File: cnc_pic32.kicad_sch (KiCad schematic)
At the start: 0 parts

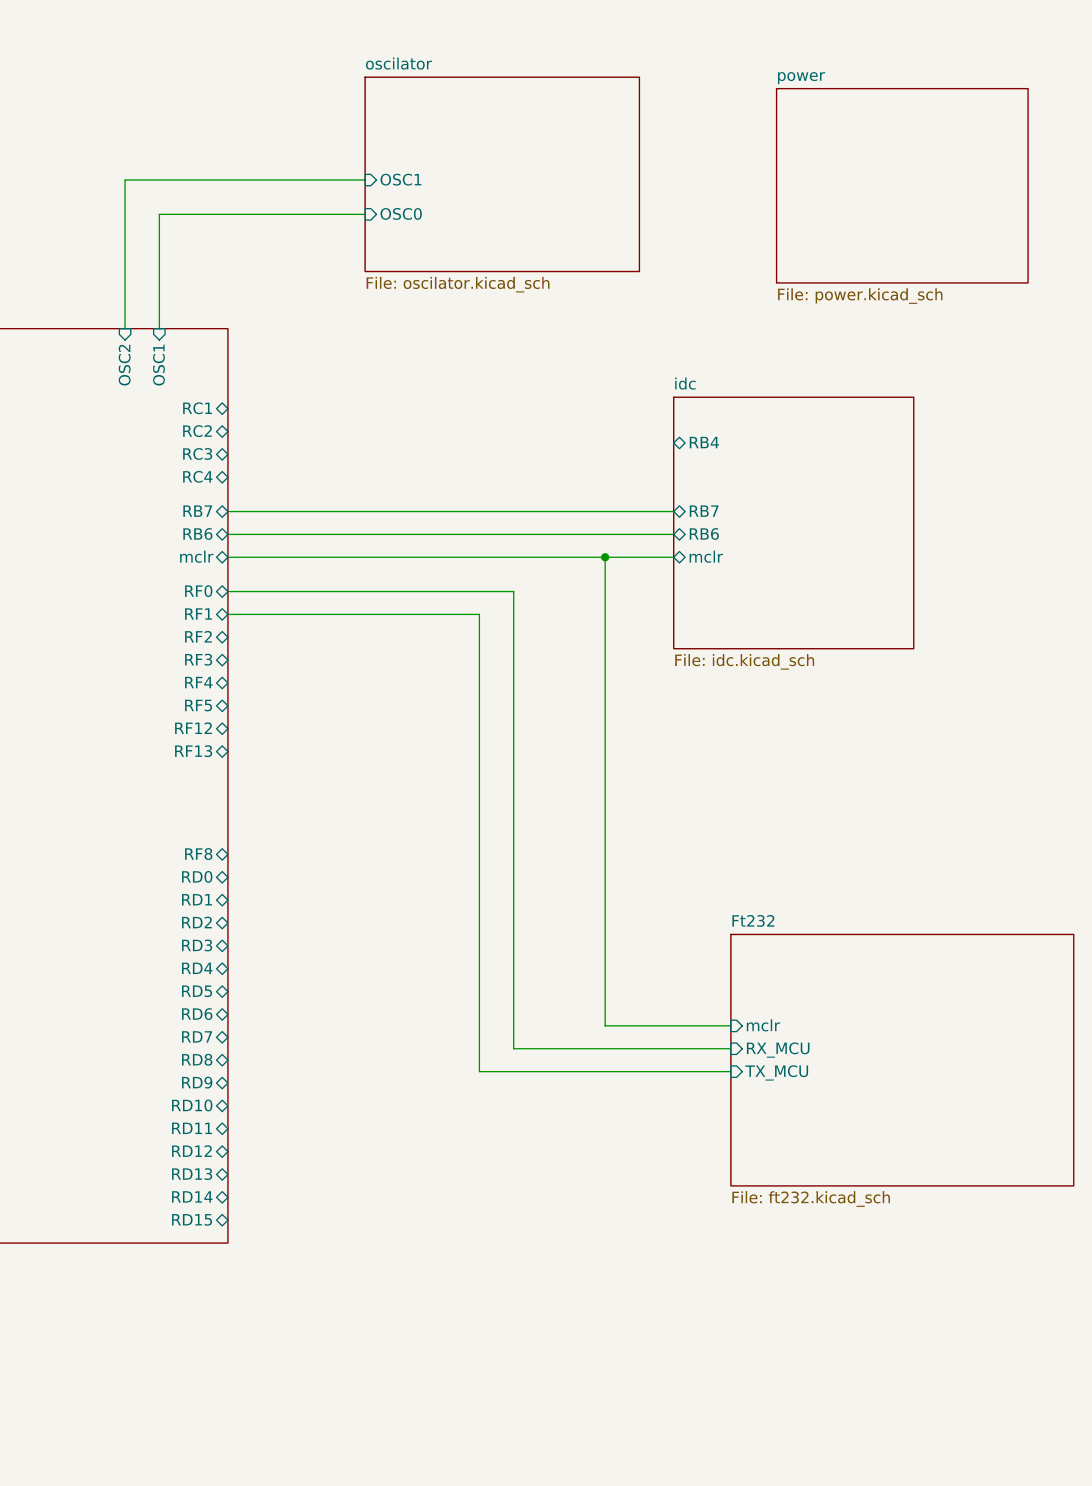
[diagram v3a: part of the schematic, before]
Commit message: feat: integrate zigbee sheet + R 0603→0805 footprint update
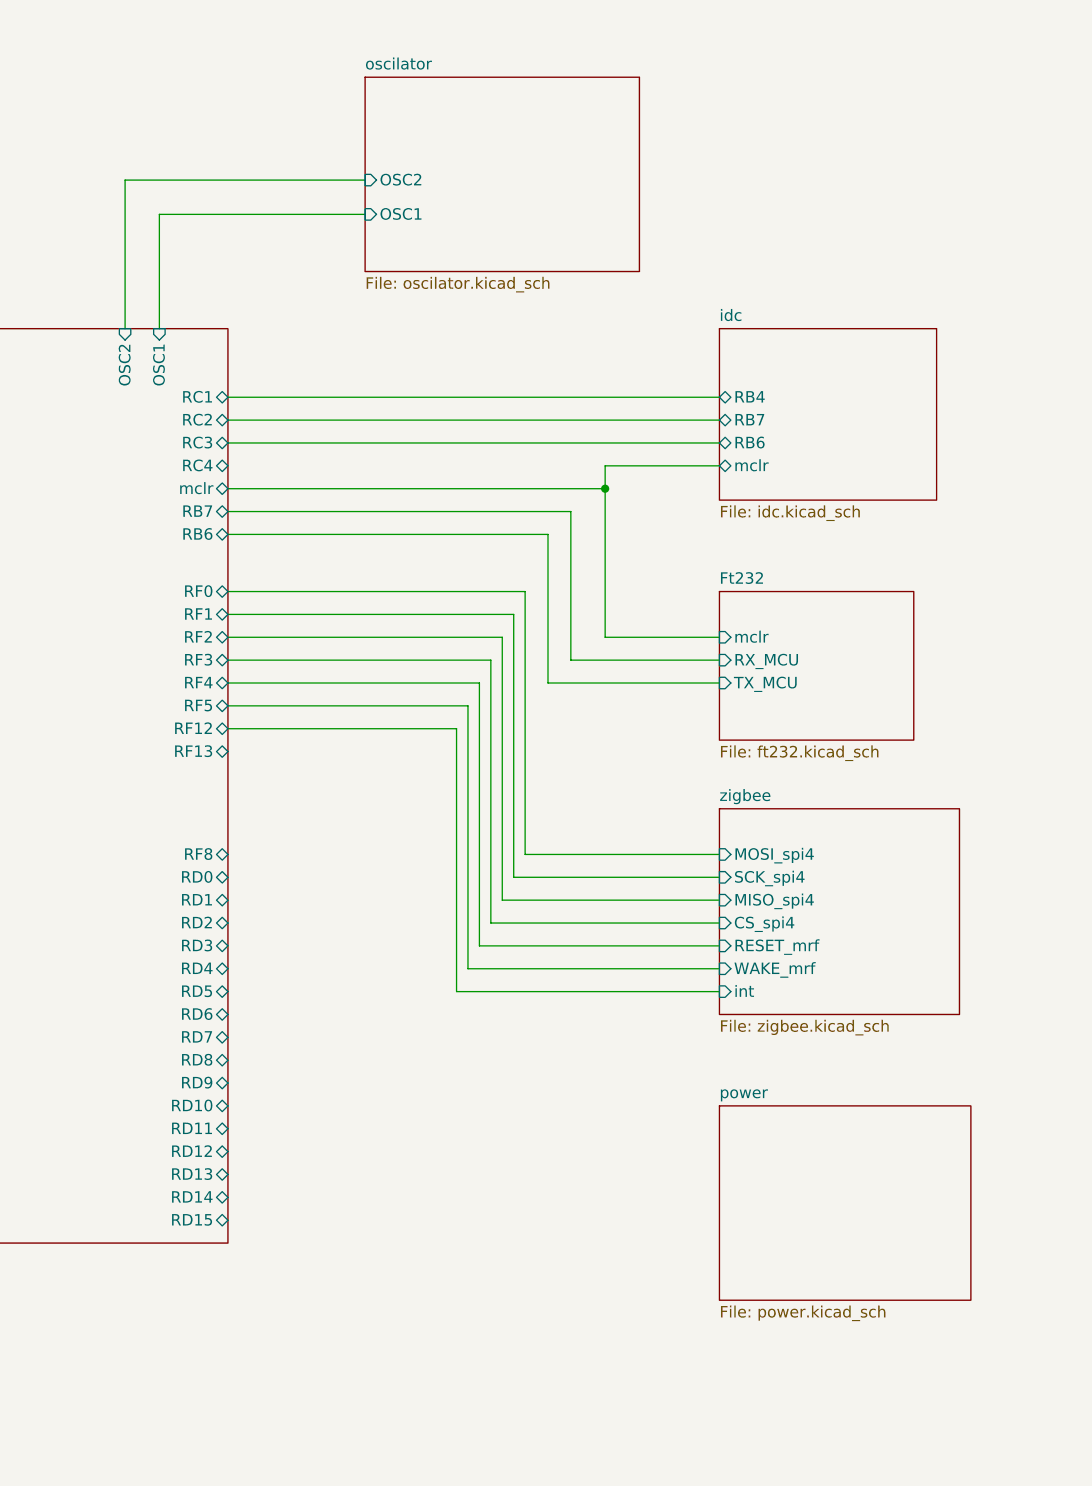
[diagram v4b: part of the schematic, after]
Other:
- added sheet zigbee (zigbee.kicad_sch)
- sheet oscilator ports: added OSC2; removed OSC0

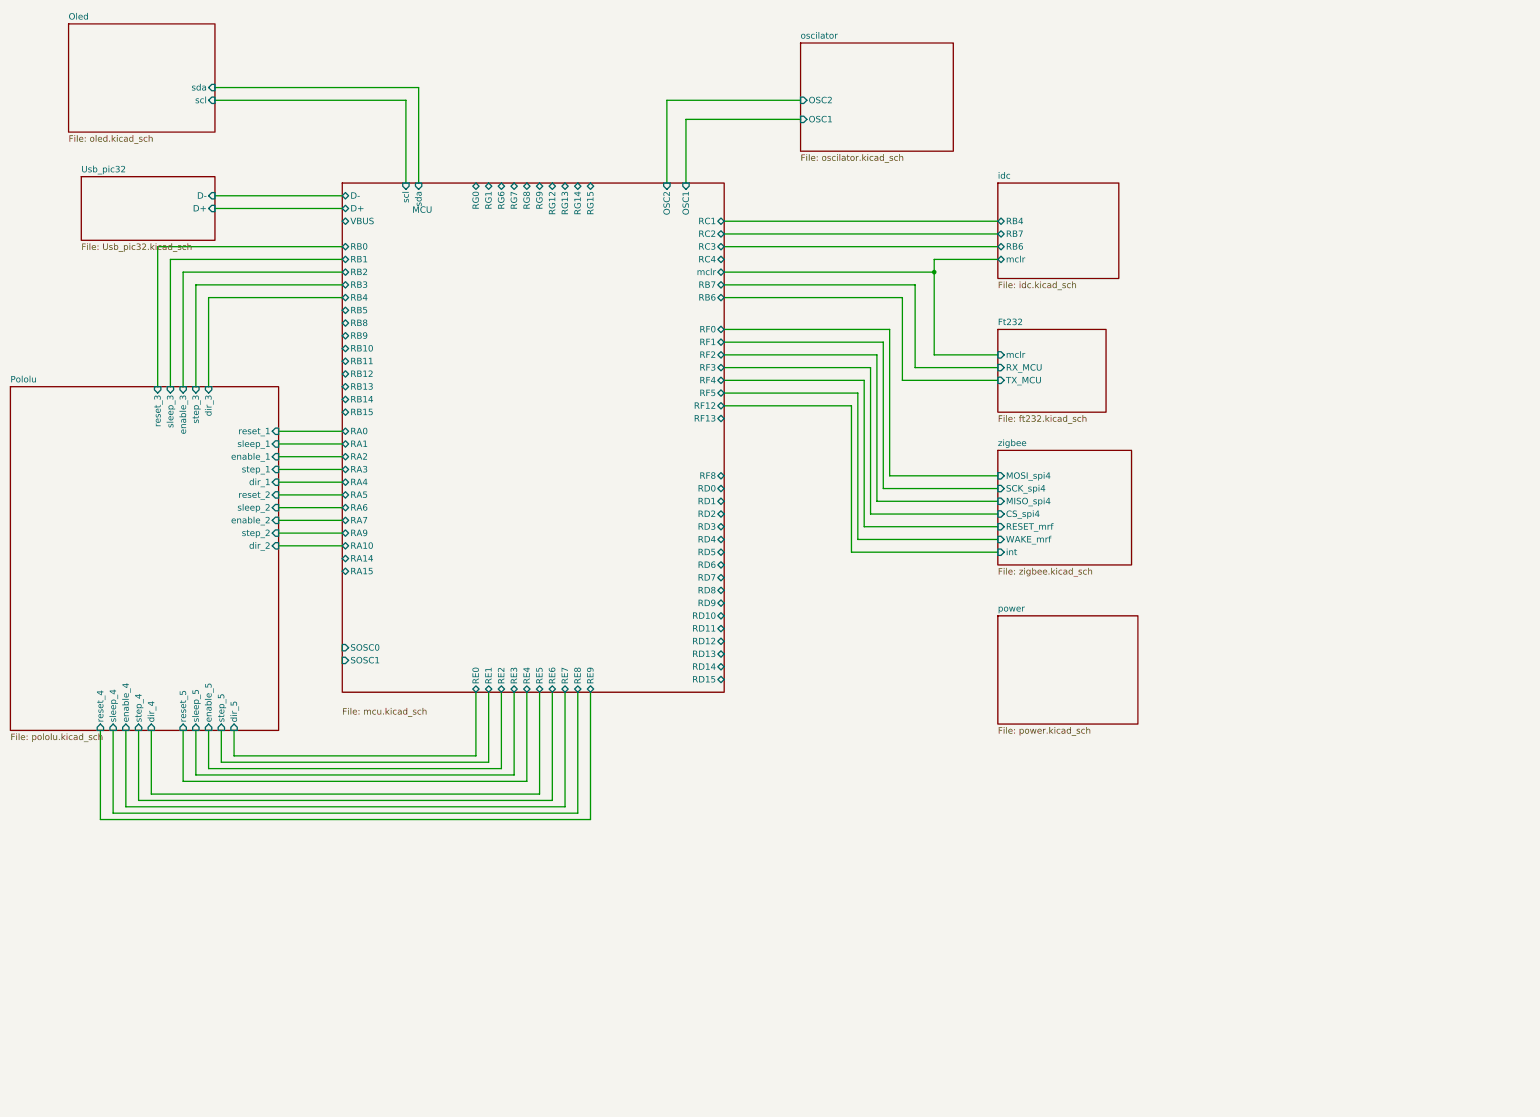
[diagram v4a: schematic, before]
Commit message: feat: 2-layer stackup, bus net class and schematic cleanup
PCB / project
- Reduce board from 4 layers to 2 (F.Cu / B.Cu) for cheaper fabrication
- Add "bus" net class and reorder net class priorities (bus 0, usb_differential 1, ...)

Schematics
- usb_conector_Ft232: add D+ / D-- labels on the USB mini-B data pair
- ft232: add 10K pull-ups, 100nf decoupling and test points on +3.3VA
- tp_ft232: remove solder jumpers JP1/JP2 (TX_Rpi / RX_Rpi now direct)
- Usb_pic32: add C38 100nf decoupling on +5V
- oled: expand connector J25 from 7 to 8 pins
- mcu / idc / power / zigbee / buttons / cnc_pic32: annotation and net cleanup

docs
- Add USB-Mini-B pinout reference images
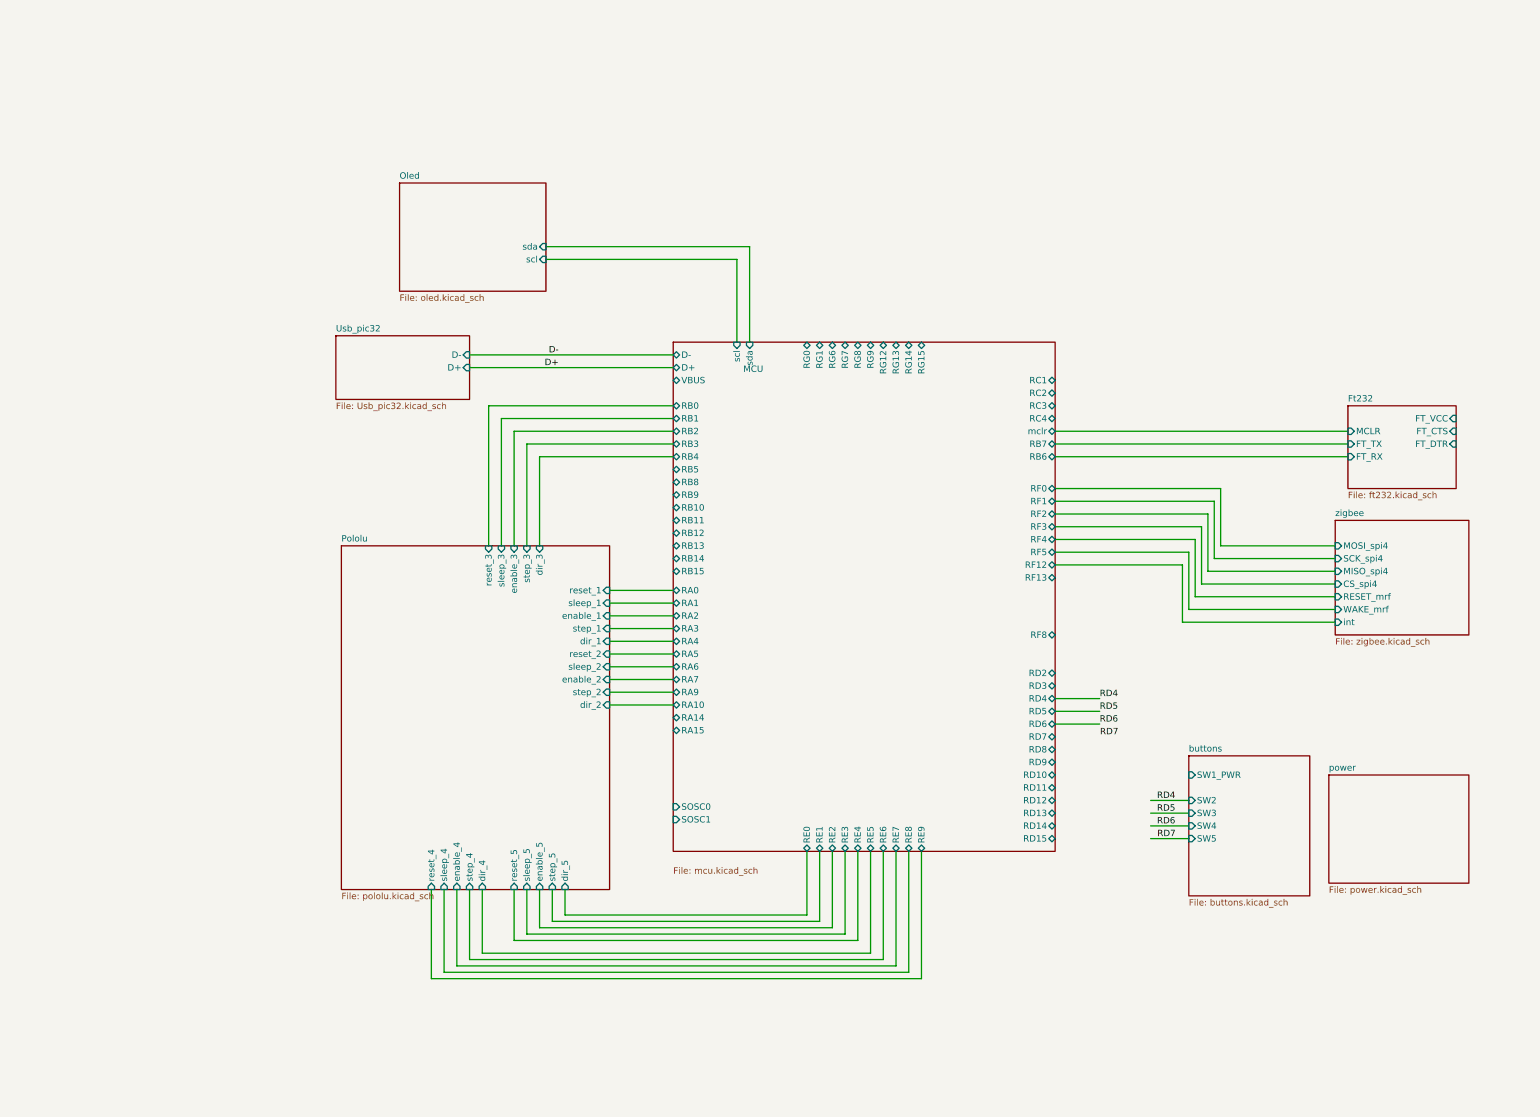
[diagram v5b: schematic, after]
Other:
- removed sheet idc
- removed sheet oscilator
- added sheet buttons (buttons.kicad_sch)
- sheet Ft232 ports: added FT_CTS, FT_DTR, FT_RX, FT_TX, FT_VCC, MCLR; removed RX_MCU, TX_MCU, mclr
- sheet MCU ports: added none; removed OSC1, OSC2, RD0, RD1

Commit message: feat: add MA240011 module sheet with labeled pins + Altium socket footprint
Esquemático
- Nueva hoja hija MA240011.kicad_sch (módulo PIC32 TQFP-100) referenciada
  desde la hoja MA240011 de mcu.kicad_sch
- mcu.kicad_sch: los 83 pines jerárquicos de MA240011 quedan rotulados con un
  label local del mismo nombre; 81 de ellos con un tramo de wire de 2.54 mm
  (un label solo no conecta a un pin de hoja) y RD4/RD5 sobre el wire existente
- mcu.kicad_sch: borde derecho del sheet 104.775 -> 106.68 mm y sus 41 pines,
  para quedar en grilla de 1.27 mm (evita 41 avisos endpoint_off_grid)
- ERC: 341 -> 158 violaciones; pin_not_connected 120 -> 39,
  isolated_pin_label 113 -> 10, endpoint_off_grid 6 -> 6
- power / zigbee / oled / pololu / cnc_pic32: pines MS1-MS3, conectores y
  anotacion de netnames

PCB
- Referencia de los 132 footprints a size 0.8 x 0.8 mm y thickness 0.12 mm
  (render_cache obsoleto eliminado para forzar el re-render)

Footprints
- lib/altium.pretty/MA240011_Socket_TQFP100_100pin.kicad_mod: zocalo adaptador
  de 100 pines TH pitch 1.27 mm convertido desde altium/Multimedia/MM20141127.PcbDoc
  (J4, patron MA240011); pads girados 90 grados sentido horario
- fp-lib-table: alta de la biblioteca "altium" (${KIPRJMOD}/lib/altium.pretty)

.gitignore
- Ignorar altium/, tmp/ y *.bkp (backups de KiCad)
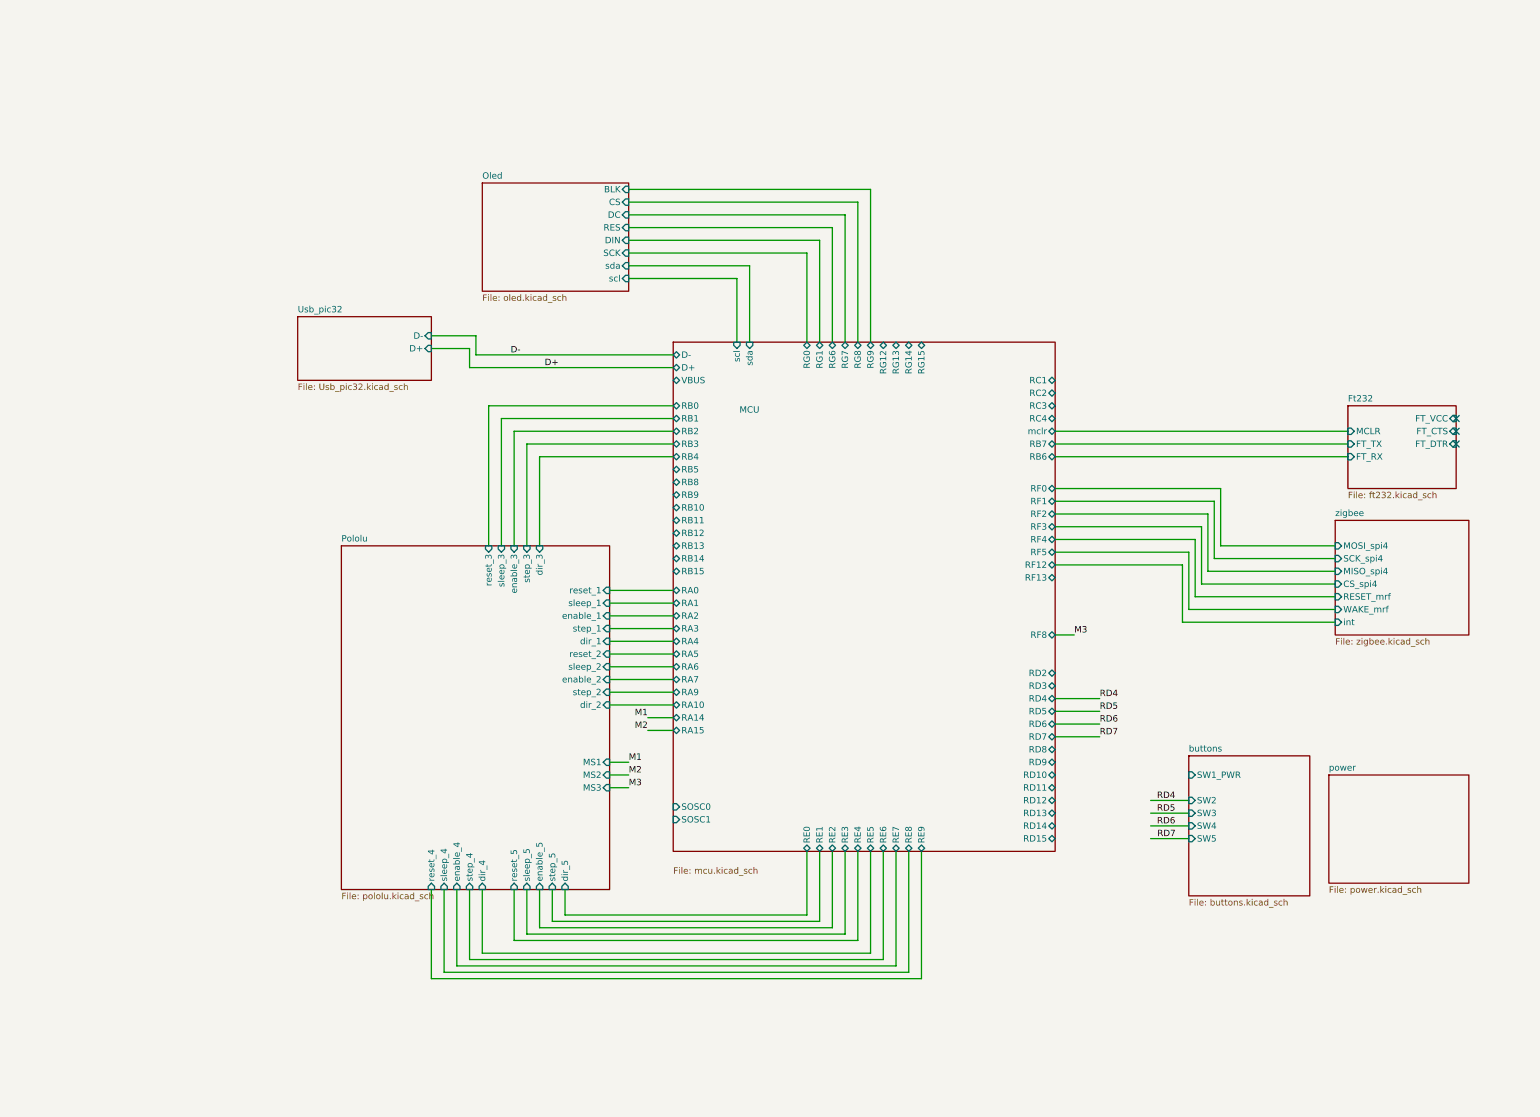
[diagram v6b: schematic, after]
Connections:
- no-connect marks 0 -> 3
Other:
- sheet Oled ports: added BLK, CS, DC, DIN, RES, SCK; removed none
- sheet Pololu ports: added MS1, MS2, MS3; removed none

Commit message: add files
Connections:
- no-connect marks 3 -> 32
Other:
- sheet zigbee renamed Radio
- sheet MCU ports: added RD0, RD1; removed scl, sda
- sheet Radio ports: added RXD_ESP8266, TXD_ESP8266; removed none

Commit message: updated
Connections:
- no-connect marks 32 -> 24
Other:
- added sheet microSD (microSD.kicad_sch)
- sheet MCU ports: added RC4_SDI1, RD0_SDO1, RD10_SCK1, RD14_SS3, RD15_SCK3, RF12_SS4, RF13_SCK4, RF2_SDI3, RF3_USBID, RF4_SDO4, RF5_SDI4, RF8_SDO3, RG7_U3RX, RG8_U3TX; removed RC4, RD0, RD10, RD14, RD15, RF12, RF13, RF2, RF3, RF4, RF5, RF8, RG7, RG8
- sheet Oled ports: added scl_i2c_1, scl_i2c_2, sda_i2c_1, sda_i2c_2; removed scl, sda
- sheet Pololu ports: added FLT_1, FLT_2, FLT_3, FLT_4, FLT_5, reset, sleep; removed reset_1, reset_2, reset_3, reset_4, reset_5, sleep_1, sleep_2, sleep_3, sleep_4, sleep_5
- sheet Radio ports: added CS_esp8266, MISO_esp8266, MOSI_esp8266, SCK_esp8266; removed CS_spi4, MISO_spi4, MOSI_spi4, SCK_spi4
- sheet Usb_pic32 ports: added ID, VBUS; removed none
- sheet buttons ports: added led1, led2, led3; removed none
